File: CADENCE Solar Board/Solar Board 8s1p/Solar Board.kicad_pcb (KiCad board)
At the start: 2 copper layers, 100 x 340.4 mm, 28 parts, among them J1 Conn_01x08, U1 INA230AIRGTT, U2 AD7414ARTZ-1REEL7, U3 OPT3001IDNPRQ1

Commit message: Added screws
had to reline everything due to screw holes
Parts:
- added REF**: MountingHole_3.2mm_M3, MountingHole:MountingHole_3.2mm_M3, F.Cu at (44.0, 10.5)
- added REF**: MountingHole_3.2mm_M3, MountingHole:MountingHole_3.2mm_M3, F.Cu at (44.0, 327.5)
- moved R2 33.6 mm to (40.9, 6.15)
- moved R3 33.6 mm to (37.4, 6.14)
- moved TP1 33.5 mm to (65.8, 7.02)
- moved TP3 32.2 mm to (35.5, 13.5)
- moved D1 31.9 mm to (33.4, 9.07)
- moved SC 31.0 mm to (87.5, 297.3)
- moved SC 31.0 mm to (87.5, 137.3)
- moved SC 31.0 mm to (1.26, 127.3)
- moved SC 31.0 mm to (1.26, 207.3)
- moved SC 31.0 mm to (1.26, 287.3)
- moved SC 31.0 mm to (87.5, 217.3)
- moved SC 31.0 mm to (87.4, 57.3)
- moved SC 31.0 mm to (1.19, 47.2)
- moved D2 30.6 mm to (26.4, 5.06)
- moved R6 30.6 mm to (30.2, 4.56)
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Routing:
- net Net-(U2-ALERT): track 7.62 -> 21.4 mm
- net Net-(U1-ALERT): track 7.58 -> 19.3 mm, vias 0 -> 2
- net HS_I2C1_LDA: track 35.7 -> 43.4 mm, vias 5 -> 10
- net HS_I2C1_LCL: track 33.2 -> 26.9 mm, vias 2 -> 6
- net Solar1+: track 26.0 -> 21.7 mm, vias 2 -> 0
- net Net-(U2-AS): track 3.67 -> 5.35 mm
- net Net-(U1-V_S+): track 2.37 -> 3.71 mm
- net GND: track 0.89 -> 0.00 mm
- net Solar1-: track 14.6 -> 15.3 mm, vias 1 -> 0
- net Net-(D1-A): track 2.71 -> 3.22 mm
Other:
- board size 100 x 340.4 mm -> 88 x 338 mm

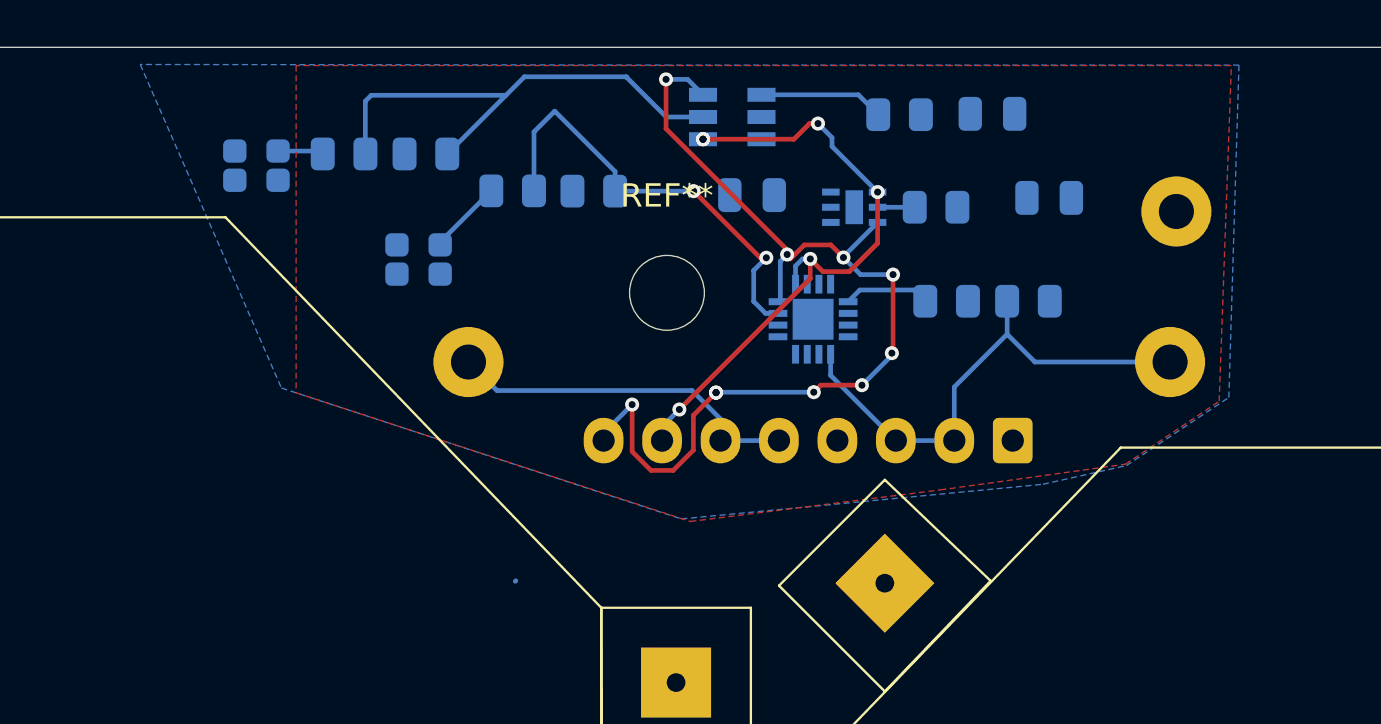
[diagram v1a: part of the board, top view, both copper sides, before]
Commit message: Updates
removed light sensor, changed pcb design, added screw holes for 8s1p and 8s2p configurations, optimized via paths in pcb
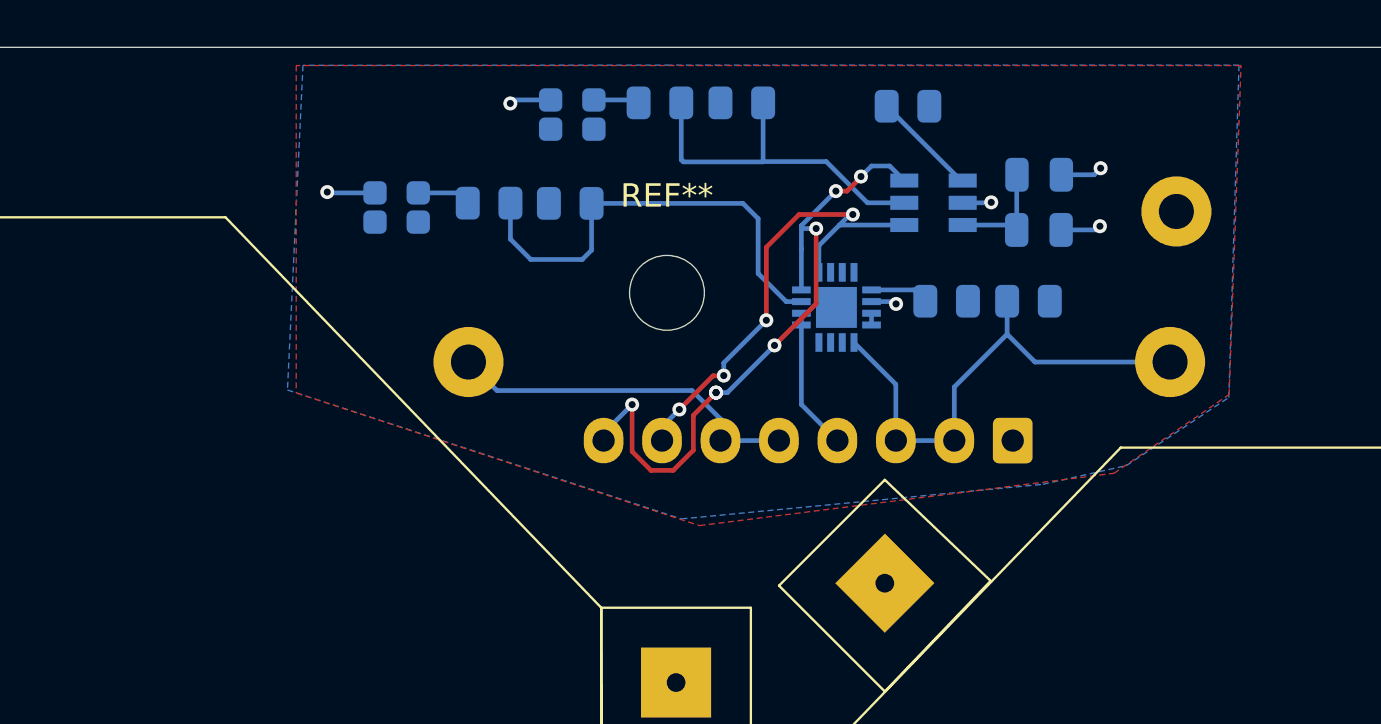
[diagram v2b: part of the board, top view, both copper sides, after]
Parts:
- removed C1: 100nF, Capacitor_SMD:C_0805_2012Metric
- removed R8: 10k, Resistor_SMD:R_0805_2012Metric
- removed U3: OPT3001IDNPRQ1, OPT3001IDNPRQ1:SON65P200X200X65-7N-D
- moved R5 13.7 mm to (47.2, 2.38)
- moved D2 13.7 mm to (40.0, 2.88)
- moved R6 13.7 mm to (43.7, 2.38)
- moved C3 12.4 mm to (59.9, 7.81), turned to 0 degrees
- moved U2 9.36 mm to (55.4, 6.65)
- moved C2 3.28 mm to (59.9, 5.45), turned to 0 degrees
- moved D1 2.41 mm to (32.4, 6.85)
- moved R3 1.14 mm to (36.4, 6.67)
- moved R2 1.14 mm to (39.9, 6.67)
- moved U1 1.12 mm to (51.2, 11.1)
- moved R7 0.51 mm to (54.3, 2.52)
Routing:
- net GND: track 0.00 -> 15.9 mm, vias 0 -> 6
- net HS_I2C1_LDA: track 43.4 -> 28.9 mm, vias 10 -> 7
- net HS_I2C1_LCL: track 26.9 -> 20.6 mm, vias 6 -> 4
- net Net-(U2-ALERT): track 21.4 -> 15.3 mm
- net +3.3V: track 0.18 -> 5.26 mm
- net Net-(U3-INT): track 1.59 -> 0.00 mm
- net Net-(U1-V_S+): track 3.71 -> 2.50 mm
- net Net-(D1-A): track 3.22 -> 2.30 mm
- net Net-(U2-AS): track 5.35 -> 4.57 mm
- net Net-(U1-ALERT): track 19.3 -> 19.6 mm, vias 2 -> 0
